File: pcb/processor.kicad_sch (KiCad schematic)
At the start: 0 parts

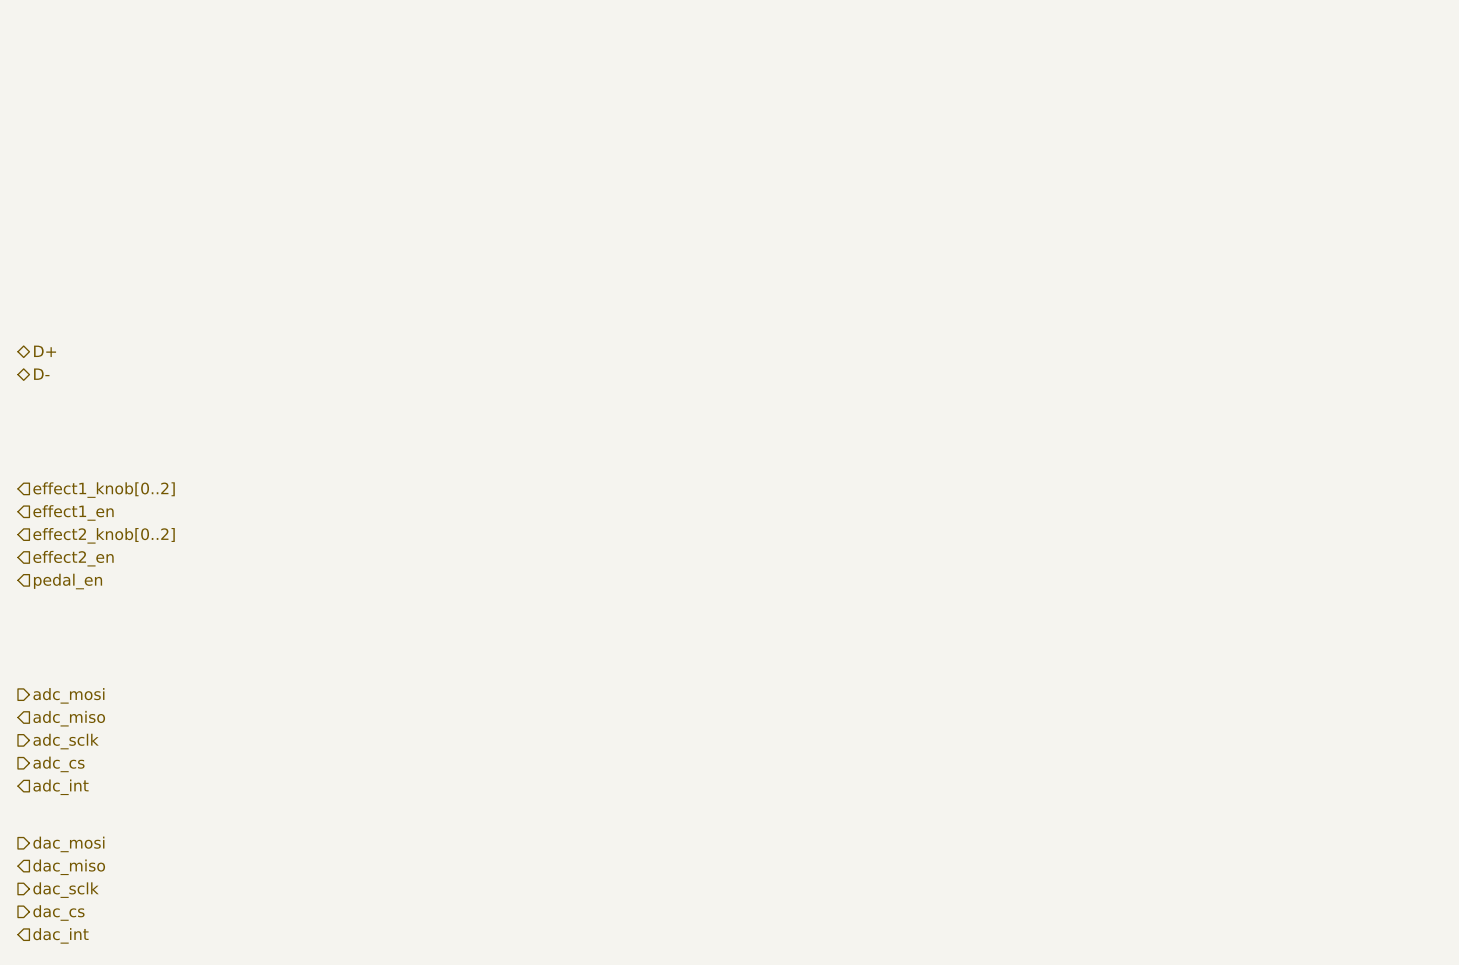
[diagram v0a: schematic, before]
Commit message: Add power supply circuit and MCU symbol.
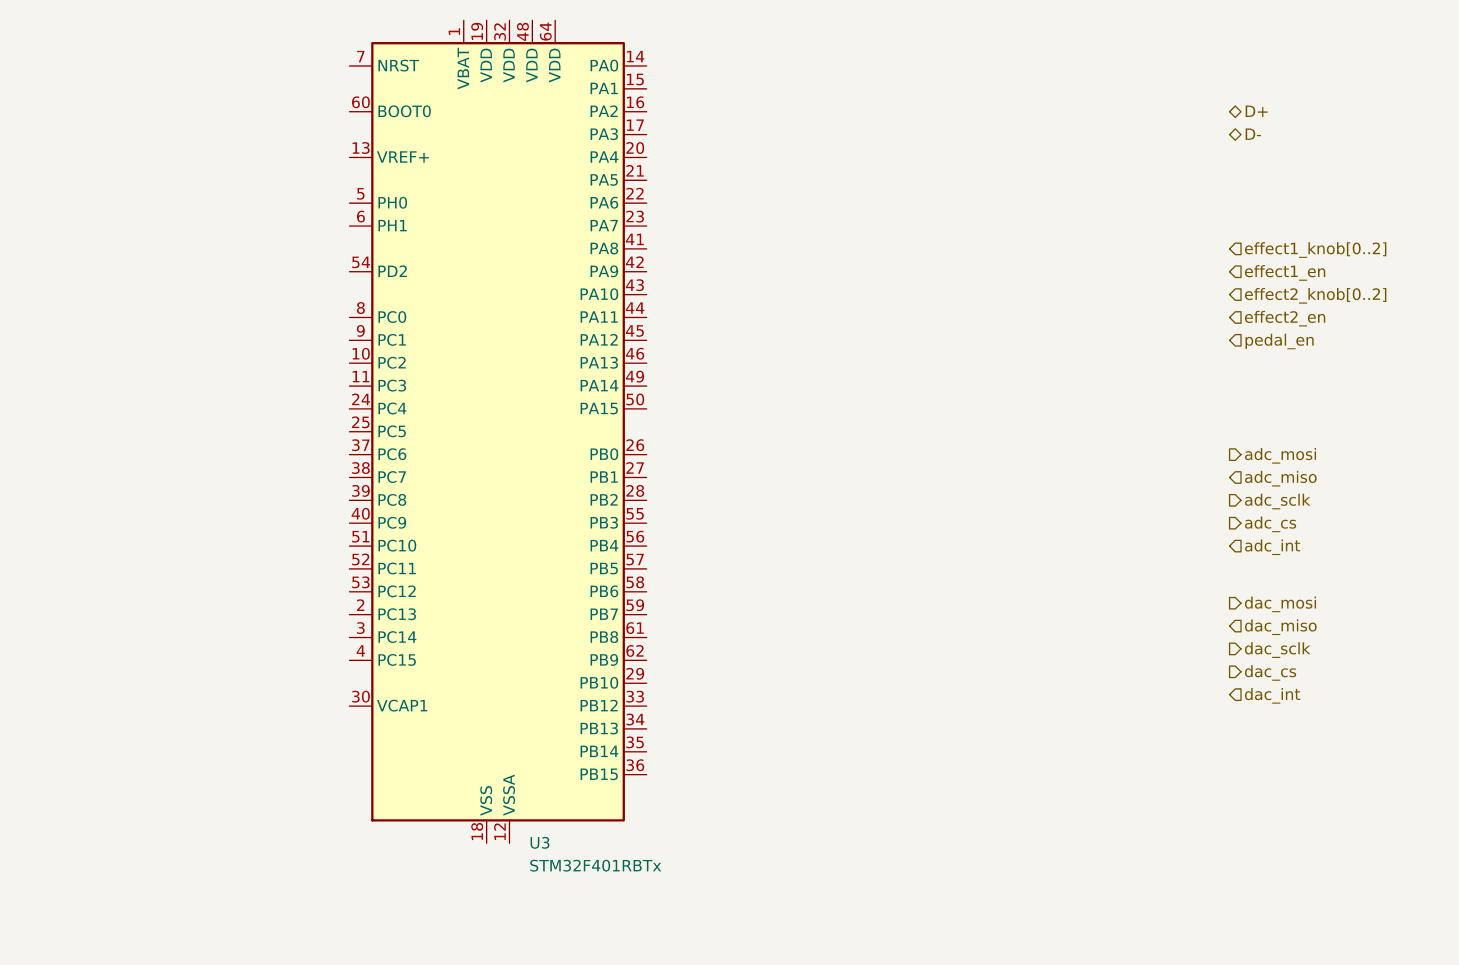
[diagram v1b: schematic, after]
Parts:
- added U3: STM32F401RBTx, Package_QFP:LQFP-64_10x10mm_P0.5mm, symbol MCU_ST_STM32F4:STM32F401RBTx
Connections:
- new net: U3.18 (VSS), U3.31 (VSS), U3.47 (VSS), U3.63 (VSS)
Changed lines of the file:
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@@
 (kicad_sch (version 20230121) (generator eeschema)
   (paper "A4")
-  (hierarchical_label "adc_int" (shape input) (at 59.69 132.08 0) (fields_autoplaced)
+  (hierarchical_label "adc_int" (shape input) (at 194.31 105.41 0) (fields_autoplaced)
     (effects (font (size 1.27 1.27)) (justify left))
   )
-  (hierarchical_label "adc_mosi" (shape output) (at 59.69 121.92 0) (fields_autoplaced)
+  (hierarchical_label "adc_mosi" (shape output) (at 194.31 95.25 0) (fields_autoplaced)
     (effects (font (size 1.27 1.27)) (justify left))
   )
-  (hierarchical_label "D-" (shape bidirectional) (at 59.69 86.36 0) (fields_autoplaced)
+  (hierarchical_label "D-" (shape bidirectional) (at 194.31 59.69 0) (fields_autoplaced)
     (effects (font (size 1.27 1.27)) (justify left))
   )
-  (hierarchical_label "adc_sclk" (shape output) (at 59.69 127 0) (fields_autoplaced)
+  (hierarchical_label "adc_sclk" (shape output) (at 194.31 100.33 0) (fields_autoplaced)
     (effects (font (size 1.27 1.27)) (justify left))
   )
-  (hierarchical_label "dac_cs" (shape output) (at 59.69 146.05 0) (fields_autoplaced)
+  (hierarchical_label "dac_cs" (shape output) (at 194.31 119.38 0) (fields_autoplaced)
     (effects (font (size 1.27 1.27)) (justify left))
   )
-  (hierarchical_label "dac_int" (shape input) (at 59.69 148.59 0) (fields_autoplaced)
+  (hierarchical_label "dac_int" (shape input) (at 194.31 121.92 0) (fields_autoplaced)
     (effects (font (size 1.27 1.27)) (justify left))
   )
-  (hierarchical_label "effect1_knob[0..2]" (shape input) (at 59.69 99.06 0) (fields_autoplaced)
+  (hierarchical_label "effect1_knob[0..2]" (shape input) (at 194.31 72.39 0) (fields_autoplaced)
     (effects (font (size 1.27 1.27)) (justify left))
   )
-  (hierarchical_label "adc_cs" (shape output) (at 59.69 129.54 0) (fields_autoplaced)
+  (hierarchical_label "adc_cs" (shape output) (at 194.31 102.87 0) (fields_autoplaced)
     (effects (font (size 1.27 1.27)) (justify left))
   )
-  (hierarchical_label "dac_sclk" (shape output) (at 59.69 143.51 0) (fields_autoplaced)
+  (hierarchical_label "dac_sclk" (shape output) (at 194.31 116.84 0) (fields_autoplaced)
     (effects (font (size 1.27 1.27)) (justify left))
   )
-  (hierarchical_label "effect1_en" (shape input) (at 59.69 101.6 0) (fields_autoplaced)
+  (hierarchical_label "effect1_en" (shape input) (at 194.31 74.93 0) (fields_autoplaced)
     (effects (font (size 1.27 1.27)) (justify left))
   )
-  (hierarchical_label "pedal_en" (shape input) (at 59.69 109.22 0) (fields_autoplaced)
+  (hierarchical_label "pedal_en" (shape input) (at 194.31 82.55 0) (fields_autoplaced)
     (effects (font (size 1.27 1.27)) (justify left))
   )
-  (hierarchical_label "dac_miso" (shape input) (at 59.69 140.97 0) (fields_autoplaced)
+  (hierarchical_label "dac_miso" (shape input) (at 194.31 114.3 0) (fields_autoplaced)
     (effects (font (size 1.27 1.27)) (justify left))
   )
-  (hierarchical_label "effect2_knob[0..2]" (shape input) (at 59.69 104.14 0) (fields_autoplaced)
+  (hierarchical_label "effect2_knob[0..2]" (shape input) (at 194.31 77.47 0) (fields_autoplaced)
     (effects (font (size 1.27 1.27)) (justify left))
   )
-  (hierarchical_label "effect2_en" (shape input) (at 59.69 106.68 0) (fields_autoplaced)
+  (hierarchical_label "effect2_en" (shape input) (at 194.31 80.01 0) (fields_autoplaced)
     (effects (font (size 1.27 1.27)) (justify left))
   )
-  (hierarchical_label "D+" (shape bidirectional) (at 59.69 83.82 0) (fields_autoplaced)
+  (hierarchical_label "D+" (shape bidirectional) (at 194.31 57.15 0) (fields_autoplaced)
     (effects (font (size 1.27 1.27)) (justify left))
   )
-  (hierarchical_label "adc_miso" (shape input) (at 59.69 124.46 0) (fields_autoplaced)
+  (hierarchical_label "adc_miso" (shape input) (at 194.31 97.79 0) (fields_autoplaced)
     (effects (font (size 1.27 1.27)) (justify left))
   )
-  (hierarchical_label "dac_mosi" (shape output) (at 59.69 138.43 0) (fields_autoplaced)
+  (hierarchical_label "dac_mosi" (shape output) (at 194.31 111.76 0) (fields_autoplaced)
     (effects (font (size 1.27 1.27)) (justify left))
   )
+  (symbol (lib_id "MCU_ST_STM32F4:STM32F401RBTx") (at 111.76 92.71 0) (unit 1)
+    (in_bom yes) (on_board yes) (dnp no) (fields_autoplaced)
+    (property "Reference" "U3" (at 116.4941 138.43 0)
+      (effects (font (size 1.27 1.27)) (justify left))
+    )
+    (property "Value" "STM32F401RBTx" (at 116.4941 140.97 0)
+      (effects (font (size 1.27 1.27)) (justify left))
+    )
+    (property "Footprint" "Package_QFP:LQFP-64_10x10mm_P0.5mm" (at 99.06 135.89 0)
+      (effects (font (size 1.27 1.27)) (justify right) hide)
+    )
+    (property "Datasheet" "https://www.st.com/resource/en/datasheet/stm32f401rb.pdf" (at 111.76 92.71 0)
+      (effects (font (size 1.27 1.27)) hide)
+    )
+    (pin "1")
+    (pin "10")
+    (pin "11")
+    (pin "12")
+    (pin "13")
+    (pin "14")
+    (pin "15")
+    (pin "16")
+    (pin "17")
+    (pin "18")
+    (pin "19")
+    (pin "2")
+    (pin "20")
+    (pin "21")
+    (pin "22")
+    (pin "23")
+    (pin "24")
+    (pin "25")
+    (pin "26")
+    (pin "27")
+    (pin "28")
+    (pin "29")
+    (pin "3")
+    (pin "30")
+    (pin "31")
+    (pin "32")
+    (pin "33")
+    (pin "34")
+    (pin "35")
+    (pin "36")
+    (pin "37")
+    (pin "38")
+    (pin "39")
+    (pin "4")
+    (pin "40")
+    (pin "41")
+    (pin "42")
+    (pin "43")
+    (pin "44")
+    (pin "45")
+    (pin "46")
+    (pin "47")
+    (pin "48")
+    (pin "49")
+    (pin "5")
+    (pin "50")
+    (pin "51")
+    (pin "52")
+    (pin "53")
+    (pin "54")
+    (pin "55")
+    (pin "56")
+    (pin "57")
+    (pin "58")
+    (pin "59")
+    (pin "6")
+    (pin "60")
+    (pin "61")
+    (pin "62")
+    (pin "63")
+    (pin "64")
+    (pin "7")
+    (pin "8")
+    (pin "9")
+    (instances
+      (project "guitar-pedal"
+        (path "/aeca30b5-691d-475f-a243-a02c48b6690c/cf1188bc-143c-43e6-988d-1de3dfdd3aac"
+          (reference "U3") (unit 1)
+        )
+      )
+    )
+  )
 )
